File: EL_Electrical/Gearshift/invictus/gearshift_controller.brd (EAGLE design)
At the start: 160 x 100 mm, 64 parts, among them IC1 MCP2562-E_SN, IC2 MCP2515-I_SO, Q1 BSS138, Q10 BSS138, Q2 BSS138, Q3 BSS138, Q4 BSS138, Q5 BSS138, Q6 BSS138, Q8 BSS123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

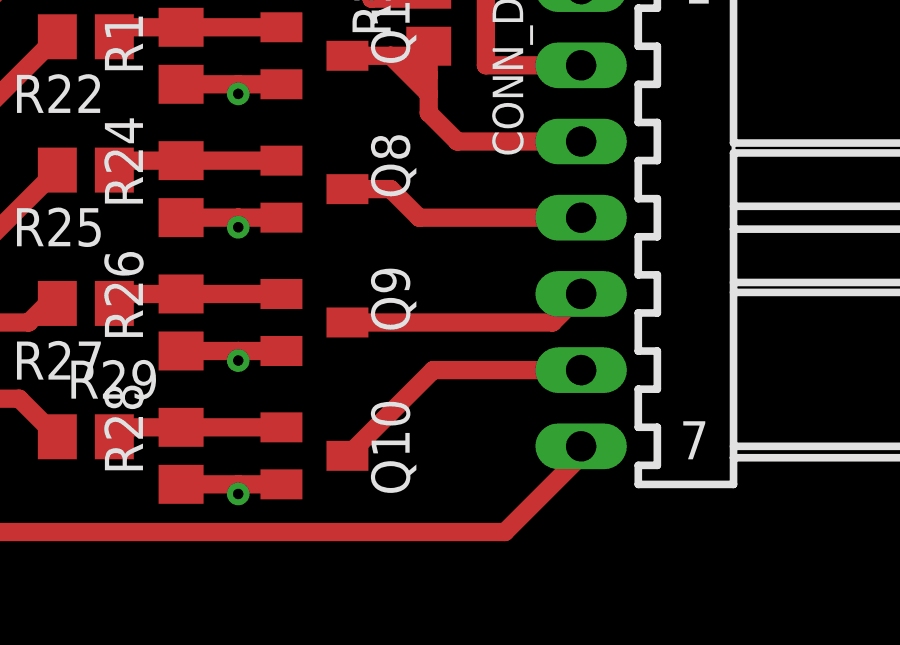
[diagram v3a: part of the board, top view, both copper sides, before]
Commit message: Add Bill of Materials (BOM) of gearshift_controller PCB without pinheaders for test points. Minor changes in names
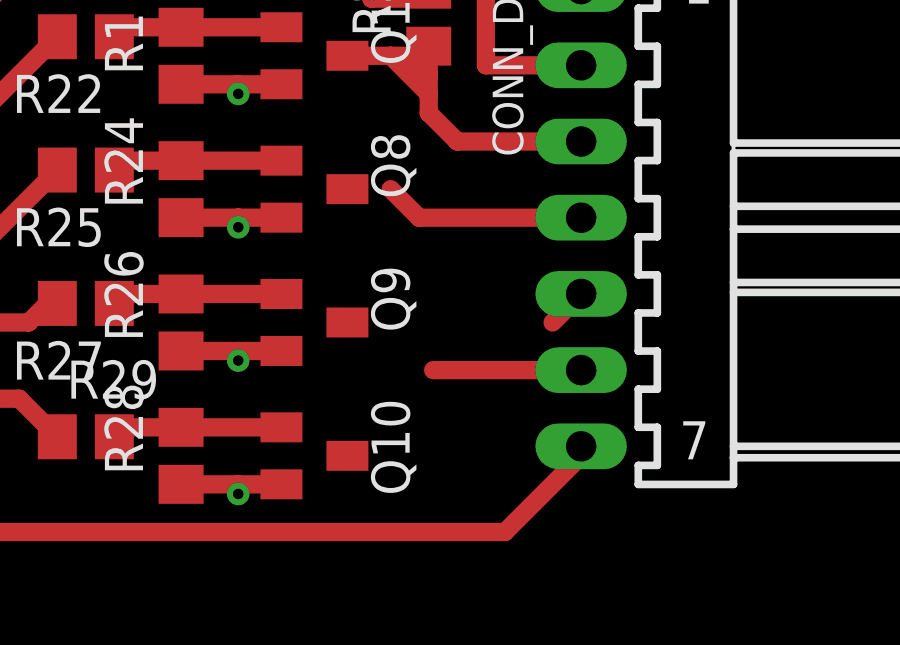
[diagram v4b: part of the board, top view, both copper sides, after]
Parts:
- Q8: value BSS123 -> BSS138
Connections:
- net LAUNCH_CONTROL_5V renamed LAUNCH_CONTROL
- net WET/DRY_5V renamed WET/DRY
- new net TRACTION_CONTROL: Q8.3
- net TRACTION_CONTROL_5V: no longer Q8.3
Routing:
- net LAUNCH_CONTROL: track 8.18 -> 1.35 mm
- net WET/DRY: track 8.97 -> 4.93 mm
- net TRACTION_CONTROL_5V: track 8.18 -> 6.74 mm
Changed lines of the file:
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@@
 <attribute name="VALUE" x="124.46" y="48.26" size="1.27" layer="27" rot="R90"/>
 </element>
-<element name="Q8" library="transistor-small-signal" library_urn="urn:adsk.eagle:library:401" package="SOT23" package3d_urn="urn:adsk.eagle:package:28738/2" value="BSS123" x="118.11" y="43.18" smashed="yes" rot="R270">
+<element name="Q8" library="transistor-small-signal" library_urn="urn:adsk.eagle:library:401" package="SOT23" package3d_urn="urn:adsk.eagle:package:28738/2" value="BSS138" x="118.11" y="43.18" smashed="yes" rot="R270">
 <attribute name="NAME" x="120.015" y="45.085" size="1.27" layer="25" rot="R270"/>
 <attribute name="POPULARITY" value="21" x="118.11" y="43.18" size="1.778" layer="27" rot="R270" display="off"/>
@@
 </signal>
 <signal name="TRACTION_CONTROL_5V">
-<contactref element="Q8" pad="3"/>
 <contactref element="CONN_DTA" pad="4"/>
 <wire x1="127" y1="42.2275" x2="121.6025" y2="42.2275" width="0.6096" layer="1"/>
 <wire x1="121.6025" y1="42.2275" x2="120.65" y2="43.18" width="0.6096" layer="1"/>
-<wire x1="120.65" y1="43.18" x2="119.21" y2="43.18" width="0.6096" layer="1"/>
 </signal>
 <signal name="LAUNCH_CONTROL_3.3V">
@@
 <wire x1="108.585" y1="38.735" x2="102.87" y2="38.735" width="0.6096" layer="1"/>
 <wire x1="108.585" y1="38.735" x2="109.22" y2="39.37" width="0.6096" layer="1"/>
-</signal>
-<signal name="LAUNCH_CONTROL_5V">
-<contactref element="Q9" pad="3"/>
-<contactref element="CONN_DTA" pad="5"/>
-<wire x1="127" y1="39.6875" x2="126.0475" y2="38.735" width="0.6096" layer="1"/>
-<wire x1="126.0475" y1="38.735" x2="119.21" y2="38.735" width="0.6096" layer="1"/>
 </signal>
 <signal name="GEAR_POT">
@@
 <wire x1="108.27" y1="36.195" x2="109.54" y2="34.925" width="0.6096" layer="1"/>
 </signal>
-<signal name="WET/DRY_5V">
+<signal name="LAUNCH_CONTROL">
+<contactref element="Q9" pad="3"/>
+<contactref element="CONN_DTA" pad="5"/>
+<wire x1="127" y1="39.6875" x2="126.0475" y2="38.735" width="0.6096" layer="1"/>
+<wire x1="119.21" y1="38.735" x2="126.0475" y2="38.735" width="0" layer="19" extent="1-1"/>
+</signal>
+<signal name="WET/DRY">
 <contactref element="Q10" pad="3"/>
 <contactref element="CONN_DTA" pad="6"/>
 <wire x1="127" y1="37.1475" x2="122.0675" y2="37.1475" width="0.6096" layer="1"/>
-<wire x1="122.0675" y1="37.1475" x2="119.21" y2="34.29" width="0.6096" layer="1"/>
+<wire x1="119.21" y1="34.29" x2="122.0675" y2="37.1475" width="0" layer="19" extent="1-1"/>
+</signal>
+<signal name="TRACTION_CONTROL">
+<contactref element="Q8" pad="3"/>
 </signal>
 </signals>

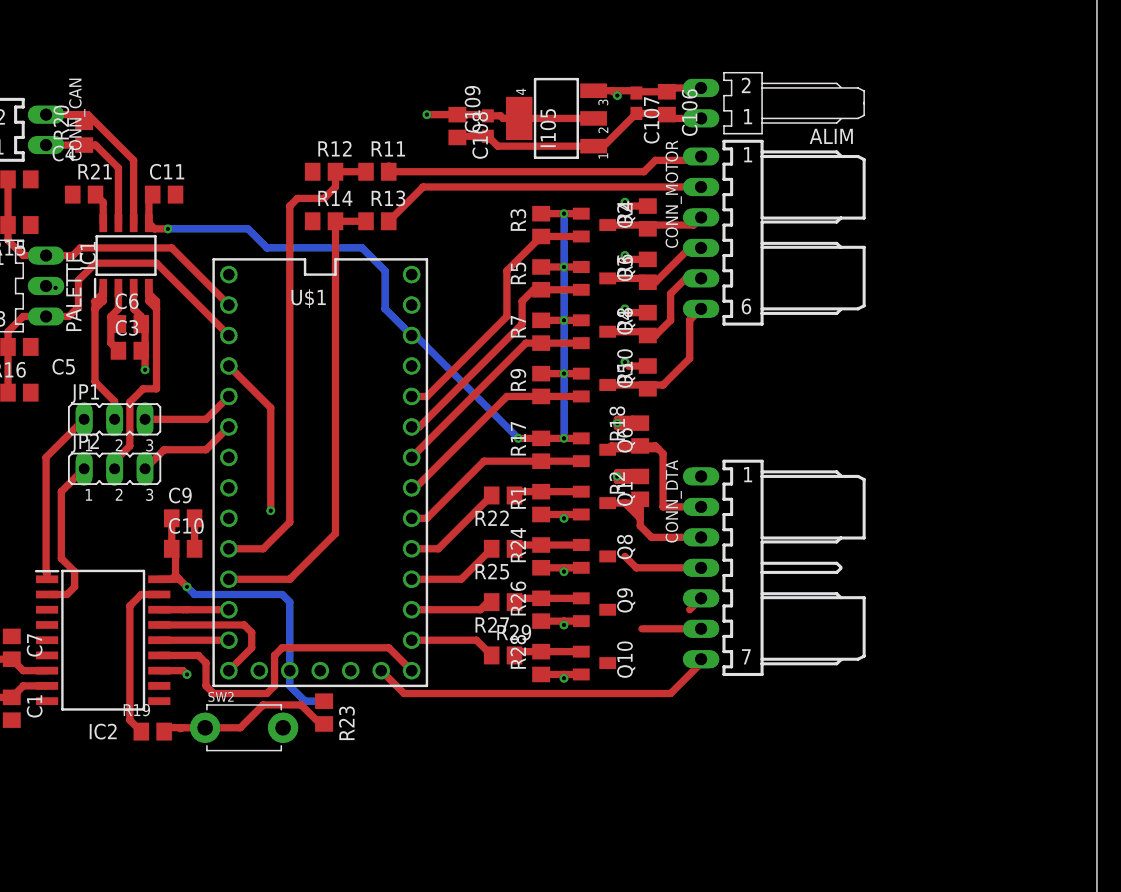
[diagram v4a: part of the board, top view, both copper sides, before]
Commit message: Add test pins
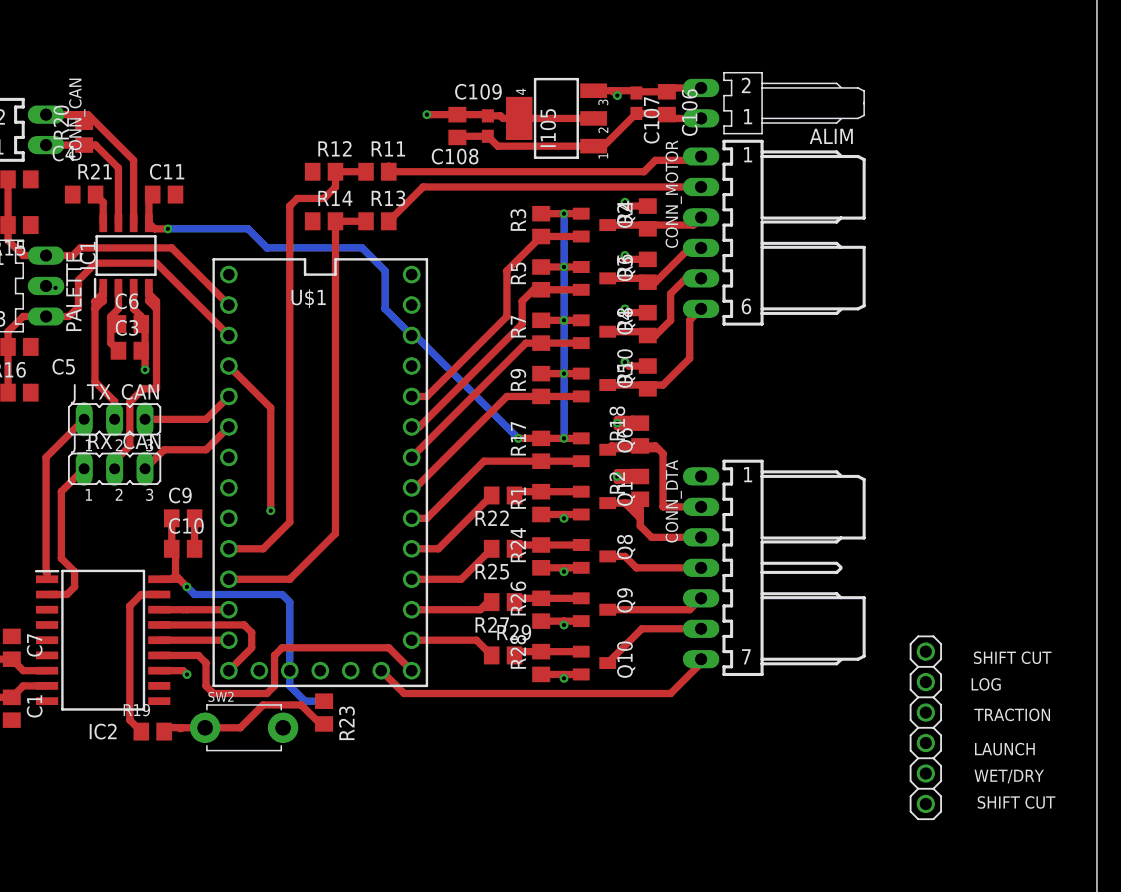
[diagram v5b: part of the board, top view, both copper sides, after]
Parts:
- added TEST_DTA: (no value), test_pin_DTA:1X06
- renumbered JP1 to J_TX_CAN, JP2 to J_RX_CAN
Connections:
- removed net TRACTION_CONTROL_5V: CONN_DTA.4
- net GEAR_POT: now also TEST_DTA.6
- net LAUNCH_CONTROL_3.3V: now also TEST_DTA.4
- net LOG_3.3V: now also TEST_DTA.2
- net SHIFT_CUT_3.3V: now also TEST_DTA.1
- net TRACTION_CONTROL: now also CONN_DTA.4
- net TRACTION_CONTROL_3.3V: now also TEST_DTA.3
- net WET/DRY_3.3V: now also TEST_DTA.5
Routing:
- net TRACTION_CONTROL: track 0.00 -> 8.18 mm
- net LAUNCH_CONTROL: track 1.35 -> 8.18 mm
- net TRACTION_CONTROL_5V: track 6.74 -> 0.00 mm
- net WET/DRY: track 4.93 -> 8.97 mm
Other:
- board text added: "LAUNCH"
- board text added: "LOG"
- board text added: "SHIFT CUT"
- board text added: "TRACTION"
- board text added: "WET/DRY"
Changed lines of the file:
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@@
 <layer number="23" name="tOrigins" color="15" fill="1" visible="yes" active="yes"/>
 <layer number="24" name="bOrigins" color="15" fill="1" visible="yes" active="yes"/>
-<layer number="25" name="tNames" color="7" fill="1" visible="no" active="yes"/>
+<layer number="25" name="tNames" color="7" fill="1" visible="yes" active="yes"/>
 <layer number="26" name="bNames" color="7" fill="1" visible="yes" active="yes"/>
 <layer number="27" name="tValues" color="7" fill="1" visible="no" active="yes"/>
@@
 <wire x1="160" y1="100" x2="0" y2="100" width="0" layer="20"/>
 <wire x1="0" y1="100" x2="0" y2="0" width="0" layer="20"/>
+<text x="156.21" y="35.2425" size="1.016" layer="25" rot="R180">SHIFT CUT
+</text>
+<text x="155.575" y="25.4" size="1.016" layer="25" rot="R180">WET/DRY</text>
+<text x="156.21" y="30.48" size="1.016" layer="25" rot="R180">TRACTION
+</text>
+<text x="152.0825" y="33.02" size="1.016" layer="25" rot="R180">LOG
+</text>
+<text x="156.5275" y="23.1775" size="1.016" layer="25" rot="R180">SHIFT CUT
+</text>
+<text x="154.94" y="27.6225" size="1.016" layer="25" rot="R180">LAUNCH
+</text>
 </plain>
 <attributes>
@@
 </element>
 <element name="C108" library="rcl" library_urn="urn:adsk.eagle:library:334" package="C0805" package3d_urn="urn:adsk.eagle:package:23617/2" value="10µ" x="106.68" y="79.0575" smashed="yes" rot="R270">
-<attribute name="NAME" x="107.95" y="80.3275" size="1.27" layer="25" rot="R270"/>
+<attribute name="NAME" x="104.4575" y="75.8825" size="1.27" layer="25"/>
 <attribute name="POPULARITY" value="88" x="29.21" y="30.7975" size="1.778" layer="27" rot="R270" display="off"/>
 <attribute name="SPICEPREFIX" value="C" x="29.21" y="30.7975" size="1.778" layer="27" rot="R270" display="off"/>
@@
 </element>
 <element name="C109" library="rcl" package="C0603" value="100n" x="109.22" y="79.0575" smashed="yes" rot="R90">
-<attribute name="NAME" x="108.585" y="78.4225" size="1.27" layer="25" rot="R90"/>
+<attribute name="NAME" x="110.49" y="82.55" size="1.27" layer="25" rot="R180"/>
 <attribute name="VALUE" x="111.125" y="78.4225" size="1.27" layer="27" rot="R90"/>
 </element>
@@
 <attribute name="VALUE" x="69.9501" y="75.3379" size="0.8128" layer="27" ratio="10" rot="R180"/>
 </element>
-<element name="JP1" library="jumper" library_urn="urn:adsk.eagle:library:252" package="JP2" package3d_urn="urn:adsk.eagle:package:15452/1" value="" x="78.105" y="54.61" smashed="yes">
+<element name="J_TX_CAN" library="jumper" library_urn="urn:adsk.eagle:library:252" package="JP2" package3d_urn="urn:adsk.eagle:package:15452/1" value="" x="78.105" y="54.61" smashed="yes">
 <attribute name="NAME" x="74.549" y="56.261" size="1.27" layer="25" ratio="10"/>
 <attribute name="POPULARITY" value="34" x="126.365" y="-15.24" size="1.778" layer="27" display="off"/>
 <attribute name="VALUE" x="74.549" y="50.292" size="1.27" layer="27" ratio="10"/>
 </element>
-<element name="JP2" library="jumper" library_urn="urn:adsk.eagle:library:252" package="JP2" package3d_urn="urn:adsk.eagle:package:15452/1" value="" x="78.105" y="50.4825" smashed="yes">
+<element name="J_RX_CAN" library="jumper" library_urn="urn:adsk.eagle:library:252" package="JP2" package3d_urn="urn:adsk.eagle:package:15452/1" value="" x="78.105" y="50.4825" smashed="yes">
 <attribute name="NAME" x="74.549" y="52.1335" size="1.27" layer="25" ratio="10"/>
 <attribute name="POPULARITY" value="34" x="135.255" y="-19.3675" size="1.778" layer="27" display="off"/>
@@
 <attribute name="SPICEPREFIX" value="R" x="95.5675" y="30.1625" size="1.778" layer="27" rot="R270" display="off"/>
 <attribute name="VALUE" x="93.0275" y="30.7975" size="1.27" layer="27" rot="R270"/>
+</element>
+<element name="TEST_DTA" library="test_pin_DTA" package="1X06" package3d_urn="urn:adsk.eagle:package:22472/2" value="" x="145.7325" y="28.8925" smashed="yes" rot="R270">
+<attribute name="NAME" x="147.5613" y="37.8587" size="1.27" layer="25" ratio="10" rot="R270" display="off"/>
+<attribute name="POPULARITY" value="79" x="145.7325" y="28.8925" size="1.778" layer="27" rot="R270" display="off"/>
+<attribute name="VALUE" x="142.5575" y="37.7825" size="1.27" layer="27" rot="R270"/>
 </element>
 </elements>
@@
 <wire x1="104.14" y1="46.355" x2="102.87" y2="46.355" width="0.6096" layer="1"/>
 <wire x1="117.01" y1="51.12" x2="113.665" y2="51.12" width="0.6096" layer="1"/>
+<contactref element="TEST_DTA" pad="1"/>
+<wire x1="117.01" y1="51.12" x2="145.7325" y2="35.2425" width="0" layer="19" extent="1-1"/>
 </signal>
 <signal name="OUT1_12V">
@@
 </signal>
 <signal name="CAN-TXD-SOFTWARE">
-<contactref element="JP1" pad="1"/>
+<contactref element="J_TX_CAN" pad="1"/>
 <contactref element="IC2" pad="1"/>
 <wire x1="72.4775" y1="41.275" x2="72.4775" y2="41.8225" width="0.6096" layer="1"/>
@@
 </signal>
 <signal name="CAN-RXD_SOFTWARE">
-<contactref element="JP2" pad="1"/>
+<contactref element="J_RX_CAN" pad="1"/>
 <contactref element="IC2" pad="2"/>
 <wire x1="73.66" y1="48.5775" x2="73.66" y2="43.02125" width="0.6096" layer="1"/>
@@
 </signal>
 <signal name="RX_CAN">
-<contactref element="JP2" pad="2"/>
+<contactref element="J_RX_CAN" pad="2"/>
 <contactref element="IC1" pad="4"/>
 <wire x1="78.105" y1="50.4825" x2="78.105" y2="51.1175" width="0.6096" layer="1"/>
@@
 </signal>
 <signal name="CAN-TX_HARDWARE">
-<contactref element="JP1" pad="3"/>
+<contactref element="J_TX_CAN" pad="3"/>
 <contactref element="U$1" pad="3"/>
 <wire x1="87.63" y1="56.515" x2="85.725" y2="54.61" width="0.6096" layer="1"/>
@@
 </signal>
 <signal name="CAN-RX_HARDWARE">
-<contactref element="JP2" pad="3"/>
+<contactref element="J_RX_CAN" pad="3"/>
 <contactref element="U$1" pad="4"/>
 <wire x1="87.63" y1="53.975" x2="85.725" y2="52.07" width="0.6096" layer="1"/>
@@
 </signal>
 <signal name="TX_CAN">
-<contactref element="JP1" pad="2"/>
+<contactref element="J_TX_CAN" pad="2"/>
 <wire x1="78.105" y1="56.1003" x2="78.105" y2="54.61" width="0.6096" layer="1"/>
 <contactref element="IC1" pad="1"/>
@@
 <wire x1="120.65" y1="47.625" x2="121.92" y2="46.355" width="0.6096" layer="1"/>
 </signal>
-<signal name="TRACTION_CONTROL_5V">
-<contactref element="CONN_DTA" pad="4"/>
-<wire x1="127" y1="42.2275" x2="121.6025" y2="42.2275" width="0.6096" layer="1"/>
-<wire x1="121.6025" y1="42.2275" x2="120.65" y2="43.18" width="0.6096" layer="1"/>
-</signal>
 <signal name="LAUNCH_CONTROL_3.3V">
 <contactref element="R27" pad="2"/>
@@
 <wire x1="108.585" y1="38.735" x2="102.87" y2="38.735" width="0.6096" layer="1"/>
 <wire x1="108.585" y1="38.735" x2="109.22" y2="39.37" width="0.6096" layer="1"/>
+<contactref element="TEST_DTA" pad="4"/>
+<wire x1="109.54" y1="39.37" x2="145.7325" y2="27.6225" width="0" layer="19" extent="1-1"/>
 </signal>
 <signal name="GEAR_POT">
@@
 <wire x1="102.235" y1="31.75" x2="124.46" y2="31.75" width="0.6096" layer="1"/>
 <wire x1="100.33" y1="33.655" x2="102.235" y2="31.75" width="0.6096" layer="1"/>
+<contactref element="TEST_DTA" pad="6"/>
+<wire x1="127" y1="34.6075" x2="145.7325" y2="22.5425" width="0" layer="19" extent="1-1"/>
 </signal>
 <signal name="N$1">
@@
 <wire x1="105.095" y1="43.815" x2="109.54" y2="48.26" width="0.6096" layer="1"/>
 <wire x1="102.87" y1="43.815" x2="105.095" y2="43.815" width="0.6096" layer="1"/>
+<contactref element="TEST_DTA" pad="2"/>
+<wire x1="109.54" y1="48.26" x2="145.7325" y2="32.7025" width="0" layer="19" extent="1-1"/>
 </signal>
 <signal name="N$8">
@@
 <wire x1="107" y1="41.275" x2="109.54" y2="43.815" width="0.6096" layer="1"/>
 <wire x1="102.87" y1="41.275" x2="107" y2="41.275" width="0.6096" layer="1"/>
+<contactref element="TEST_DTA" pad="3"/>
+<wire x1="109.54" y1="43.815" x2="145.7325" y2="30.1625" width="0" layer="19" extent="1-1"/>
 </signal>
 <signal name="N$9">
@@
 <wire x1="102.87" y1="36.195" x2="108.27" y2="36.195" width="0.6096" layer="1"/>
 <wire x1="108.27" y1="36.195" x2="109.54" y2="34.925" width="0.6096" layer="1"/>
+<contactref element="TEST_DTA" pad="5"/>
+<wire x1="109.54" y1="34.925" x2="145.7325" y2="25.0825" width="0" layer="19" extent="1-1"/>
 </signal>
 <signal name="LAUNCH_CONTROL">
 <contactref element="Q9" pad="3"/>
 <contactref element="CONN_DTA" pad="5"/>
-<wire x1="127" y1="39.6875" x2="126.0475" y2="38.735" width="0.6096" layer="1"/>
-<wire x1="119.21" y1="38.735" x2="126.0475" y2="38.735" width="0" layer="19" extent="1-1"/>
+<wire x1="126.0475" y1="38.735" x2="127" y2="39.6875" width="0.6096" layer="1"/>
+<wire x1="119.21" y1="38.735" x2="126.0475" y2="38.735" width="0.6096" layer="1"/>
 </signal>
 <signal name="WET/DRY">
 <contactref element="Q10" pad="3"/>
 <contactref element="CONN_DTA" pad="6"/>
-<wire x1="127" y1="37.1475" x2="122.0675" y2="37.1475" width="0.6096" layer="1"/>
-<wire x1="119.21" y1="34.29" x2="122.0675" y2="37.1475" width="0" layer="19" extent="1-1"/>
+<wire x1="122.0675" y1="37.1475" x2="127" y2="37.1475" width="0.6096" layer="1"/>
+<wire x1="119.21" y1="34.29" x2="122.0675" y2="37.1475" width="0.6096" layer="1"/>
 </signal>
 <signal name="TRACTION_CONTROL">
 <contactref element="Q8" pad="3"/>
+<contactref element="CONN_DTA" pad="4"/>
+<wire x1="127" y1="42.2275" x2="121.6025" y2="42.2275" width="0.6096" layer="1"/>
+<wire x1="120.65" y1="43.18" x2="121.6025" y2="42.2275" width="0.6096" layer="1"/>
+<wire x1="119.21" y1="43.18" x2="120.65" y2="43.18" width="0.6096" layer="1"/>
 </signal>
 </signals>
@@
 </drawing>
 <compatibility>
+<note version="6.3" minversion="6.2.2" severity="warning">
+Since Version 6.2.2 text objects can contain more than one line,
+which will not be processed correctly with this version.
+</note>
 <note version="8.2" severity="warning">
 Since Version 8.2, EAGLE supports online libraries. The ids
